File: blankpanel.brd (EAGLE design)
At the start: 140 x 183 mm, 100 parts, among them J1 S1911-46R, J3 S1911-46R, Q1 NDS8434, Q2 NDS8434, U1 ATWINC, U2 INA219, U3 ATWINC, U4 MCP7384X, U5 INA219, U6 MCP7384X

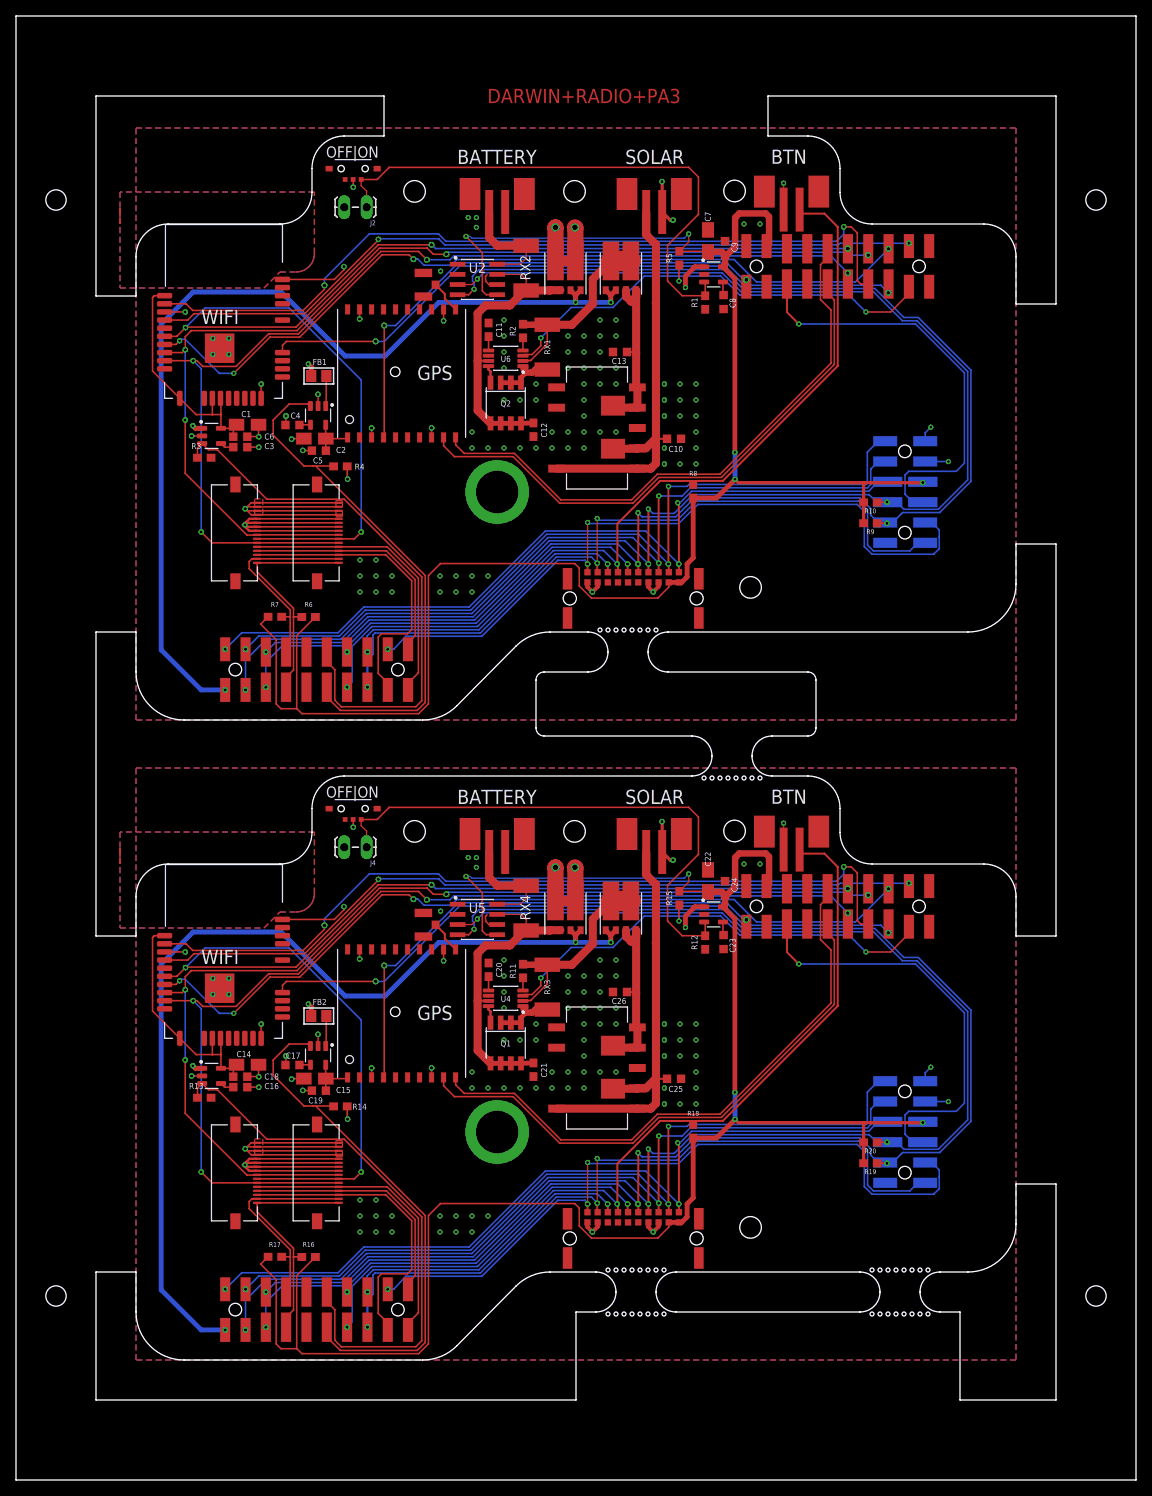
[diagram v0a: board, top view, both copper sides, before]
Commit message: Removed unwanted panel files and changed unpopulated panel template.
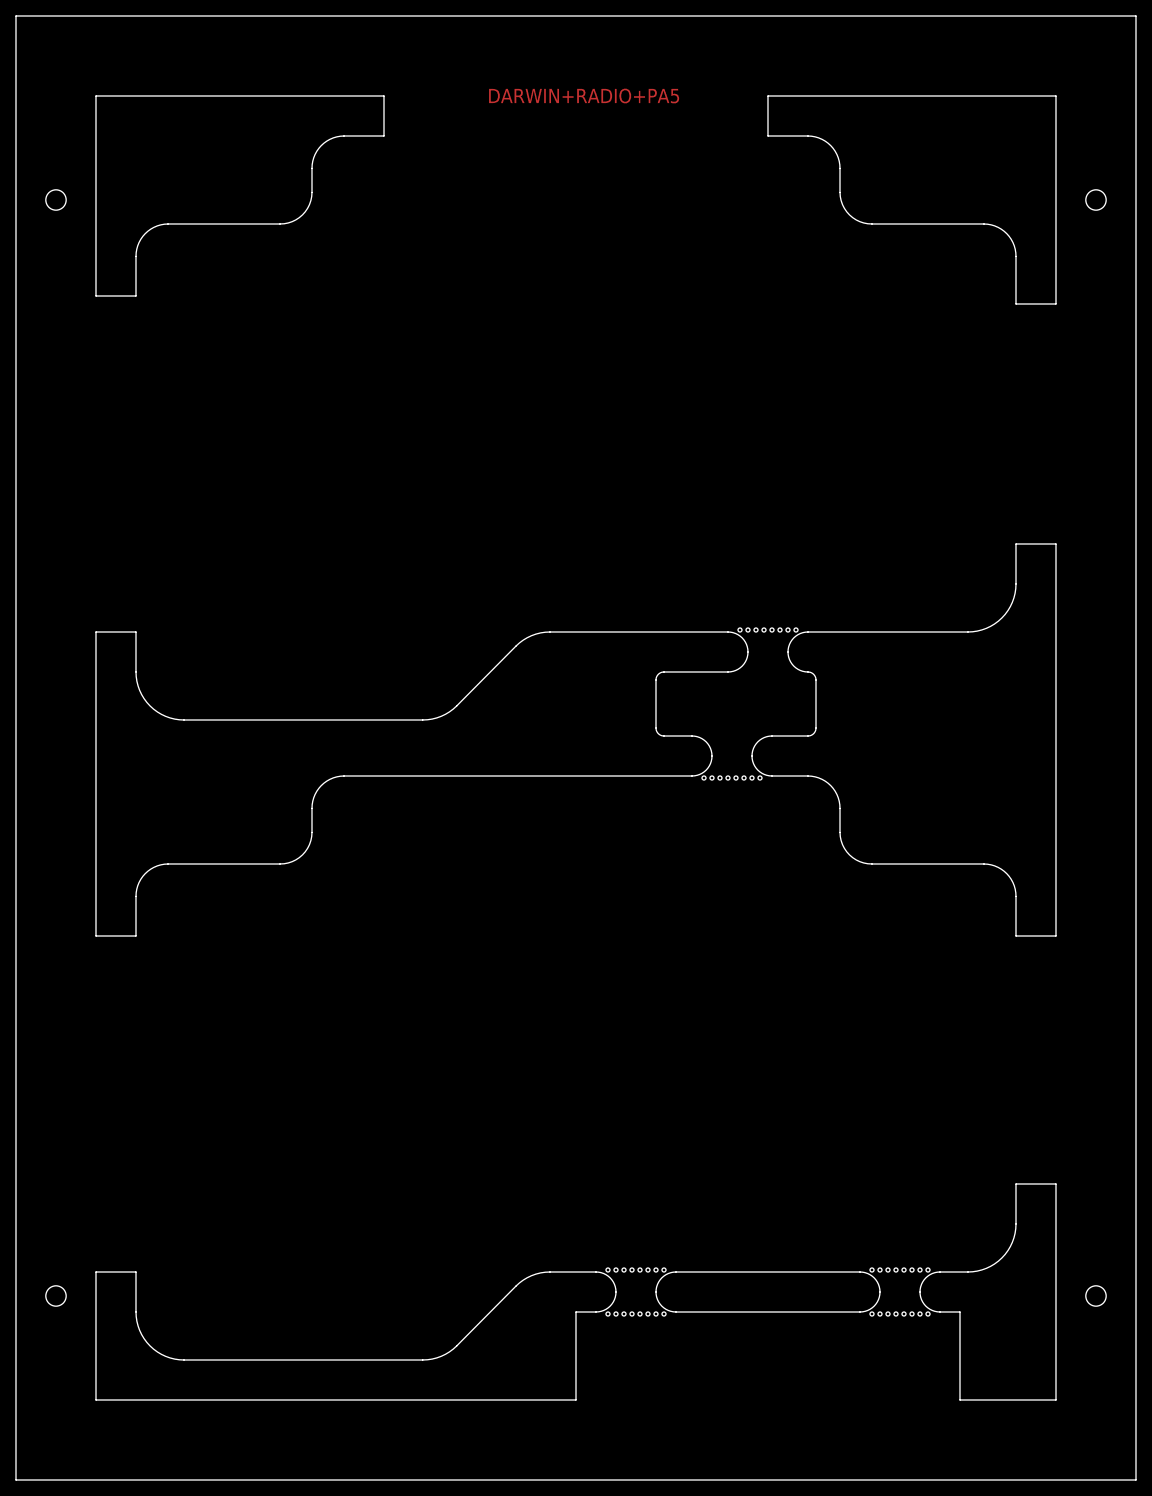
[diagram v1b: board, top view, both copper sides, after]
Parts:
- removed BACKPACK, BACKPACK1: 2X6-HEADERSDS, Conservify:12PH
- removed BACKPLANE, BACKPLANE1: M55-6102042R, Conservify:M55-6102042R
- removed BAT-JST, BAT-JST1, BTN-JST, BTN-JST1, SOLAR-JST, SOLAR-JST1: B2B-PH-SM4-TB, Conservify:B2B-PH-SM4-TB
- removed C1, C14, C15, C2, C22, C7: 6.8uf, rcl:A/3216-18R
- removed C10, C13, C25, C26: 22uf, rcl:C0603K
- removed C11, C20: 0.1uF, SparkFun-Capacitors:0603
- removed C12, C21: 10uF, SparkFun-Capacitors:0603
- removed C16, C17, C23, C3, C4, C8: 470pf, rcl:C0603K
- removed C18, C19, C24, C5, C6, C9: .1uf, rcl:C0603K
- removed D1, D2, D3, D4: V10KL45DUHM3/H, Conservify:V10KL45DUHM3/H
- removed FB1, FB2: (no value), microbuilder:0805
- removed FFC1, FFC2, FFC3, FFC4: 505110-1692, Conservify:505110-1692
- removed J1, J3: S1911-46R, Conservify:S1911-46R
- removed J2, J4: (no value), SparkFun-Connectors:1X02_LOCK_LONGPADS
- removed LOWER1, LOWER2, UPPER1, UPPER2: MOLEX-15-91-2200, Conservify:20PH
- removed Q1, Q2: NDS8434, Conservify:SO08-IRF
- removed R1, R10, R11, R12, R13, R14, R15, R16, R17, R18, R19, R2, R20, R3, R4, R5, R6, R7, R8, R9: 100k, SparkFun-Resistors:0603
- removed REG1, REG2: V78E06-1000-SMT-TR, Conservify:V78E06-1000-SMT-TR
- removed RX1, RX2, RX3, RX4: 100M, rcl:R2512
- removed U$1, U$6: FGPMMOPA6H, Conservify:GPS_MODULE
- removed U$10, U$5: SSAJ110100, Conservify:SSAJ110100
- removed U$11, U$12: 2337019-1, Conservify:2337019-1
- removed U$2, U$3, U$4, U$7, U$8, U$9: MIC5219-3.3YM5-TR, Conservify:SOT95P280X145-5
- removed U1, U3: ATWINC, Conservify:ATWINC
- removed U2, U5: INA219, Conservify:SOIC127P599X175-8N
- removed U4, U6: MCP7384X, Conservify:SOP65P490X110-8
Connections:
- removed net 3V1: BACKPACK1.3, BACKPLANE1.P11, BACKPLANE1.P12, C22.+, C24.1, R15.1, R16.2, R17.2, R18.1, R19.2, R20.2, U$9.5, U5.5, UPPER2.PIN19
- removed net 3V3: BACKPACK.3, BACKPLANE.P11, BACKPLANE.P12, C7.+, C9.1, R10.2, R5.1, R6.2, R7.2, R8.1, R9.2, U$4.5, U2.5, UPPER1.PIN19
- removed net BACKPACK_ENABLE: BACKPACK.4, UPPER1.PIN3
- removed net BACKPACK_ENABLE1: BACKPACK1.4, UPPER2.PIN3
- removed net BAT+: C12.1, D1.A1-1, D1.A1-2, Q2.5, Q2.6, Q2.7, Q2.8, RX2.1, U2.7, U6.7
- removed net BAT+1: C21.1, D2.A1-1, D2.A1-2, Q1.5, Q1.6, Q1.7, Q1.8, RX4.1, U4.7, U5.7
- removed net BAT+RAW: BAT-JST.+, RX2.2, U2.8
- removed net BAT+RAW1: BAT-JST1.+, RX4.2, U5.8
- removed net CHARGESUPPLY: D3.K1, D3.K2, R2.1, RX1.1, U6.2
- removed net CHARGESUPPLY1: D4.K1, D4.K2, R11.1, RX3.1, U4.2
- removed net CHARGING: R5.2, U6.3, UPPER1.PIN9
- removed net CHARGING1: R15.2, U4.3, UPPER2.PIN9
- removed net D+: LOWER1.PIN6
- removed net D+1: LOWER2.PIN6
- removed net D-: LOWER1.PIN15
- removed net D-1: LOWER2.PIN15
- removed net EEPROM_PROT: BACKPACK.5, BACKPLANE.P1, LOWER1.PIN2
- removed net EEPROM_PROT1: BACKPACK1.5, BACKPLANE1.P1, LOWER2.PIN2
- removed net GND: BACKPACK.2, BACKPLANE.P19, BACKPLANE.P20, BAT-JST.-, BTN-JST.+, C1.-, C10.2, C11.2, C12.2, C13.2, C2.-, C3.2, C4.2, C5.2, C6.2, C7.-, C8.2, C9.2, FFC1.1, FFC1.2, FFC1.3, FFC1.4, FFC2.1, FFC2.2, FFC2.3, FFC2.4, R1.1, R3.1, R4.1, REG1.P$3, REG1.P$7, SOLAR-JST.-, U$1.P$12, U$1.P$19, U$1.P$3, U$1.P$8, U$11.GND, U$11.GND2, U$2.2, U$3.2, U$4.2, U1.12, U1.28, U1.9, U1.PAD, U2.1, U2.2, U2.6, U6.6, UPPER1.PIN20
- removed net GND2: BACKPACK1.2, BACKPLANE1.P19, BACKPLANE1.P20, BAT-JST1.-, BTN-JST1.+, C14.-, C15.-, C16.2, C17.2, C18.2, C19.2, C20.2, C21.2, C22.-, C23.2, C24.2, C25.2, C26.2, FFC3.1, FFC3.2, FFC3.3, FFC3.4, FFC4.1, FFC4.2, FFC4.3, FFC4.4, R12.1, R13.1, R14.1, REG2.P$3, REG2.P$7, SOLAR-JST1.-, U$12.GND, U$12.GND2, U$6.P$12, U$6.P$19, U$6.P$3, U$6.P$8, U$7.2, U$8.2, U$9.2, U3.12, U3.28, U3.9, U3.PAD, U4.6, U5.1, U5.2, U5.6, UPPER2.PIN20
- removed net GPS_ENABLE: LOWER1.PIN16, R4.2, U$2.3
- removed net GPS_ENABLE1: LOWER2.PIN16, R14.2, U$7.3
- removed net GPS_RX: U$1.P$9, UPPER1.PIN5
- removed net GPS_RX1: U$6.P$9, UPPER2.PIN5
- removed net GPS_TX: U$1.P$10, UPPER1.PIN16
- removed net GPS_TX1: U$6.P$10, UPPER2.PIN16
- removed net HOTSWAP_INT: BACKPLANE.P3, LOWER1.PIN3
- removed net HOTSWAP_INT1: BACKPLANE1.P3, LOWER2.PIN3
- removed net MOD_G0: FFC1.13, FFC2.13, LOWER1.PIN1
- removed net MOD_G1: FFC3.13, FFC4.13, LOWER2.PIN1
- removed net MOD_G13: FFC1.14, FFC2.14, LOWER1.PIN19
- removed net MOD_G14: FFC1.12, FFC2.12, LOWER1.PIN20
- removed net MOD_G2: BACKPACK.6, BACKPLANE.P2, LOWER1.PIN18
- removed net MOD_G3: BACKPACK1.6, BACKPLANE1.P2, LOWER2.PIN18
- removed net MOD_G4: BACKPLANE1.P5, LOWER2.PIN4
- removed net MOD_G5: BACKPLANE.P5, LOWER1.PIN4
- removed net MOD_G6: FFC3.14, FFC4.14, LOWER2.PIN19
- removed net MOD_G7: FFC3.12, FFC4.12, LOWER2.PIN20
- removed net MOD_MISO: BACKPACK.10, BACKPLANE.P10, LOWER1.PIN10
- removed net MOD_MISO1: BACKPACK1.10, BACKPLANE1.P10, LOWER2.PIN10
- removed net MOD_MOSI: BACKPACK.11, BACKPLANE.P8, LOWER1.PIN12
- removed net MOD_MOSI1: BACKPACK1.11, BACKPLANE1.P8, LOWER2.PIN12
- removed net MOD_SCK: BACKPACK.12, BACKPLANE.P9, LOWER1.PIN9
- removed net MOD_SCK1: BACKPACK1.12, BACKPLANE1.P9, LOWER2.PIN9
- removed net MOD_SCL: BACKPACK.8, BACKPLANE.P6, LOWER1.PIN13, R9.1, U2.4
- removed net MOD_SCL1: BACKPACK1.8, BACKPLANE1.P6, LOWER2.PIN13, R19.1, U5.4
- removed net MOD_SDA: BACKPACK.9, BACKPLANE.P7, LOWER1.PIN8, R10.1, U2.3
- removed net MOD_SDA1: BACKPACK1.9, BACKPLANE1.P7, LOWER2.PIN8, R20.1, U5.3
- removed net N$1: C3.1, U$3.4
- removed net N$11: C17.1, U$7.4
- removed net N$12: C15.+, C19.1, U$6.P$1, U$7.5
- removed net N$13: Q1.1, Q1.2, Q1.3, RX3.2, U4.1
- removed net N$14: Q2.1, Q2.2, Q2.3, RX1.2, U6.1
- removed net N$16: Q1.4, U4.8
- removed net N$17: Q2.4, U6.8
- removed net N$18: C11.1, U6.5
- removed net N$19: C20.1, U4.5
- removed net N$2: C4.1, U$2.4
- removed net N$20: R11.2, U4.4
- removed net N$21: C23.1, U$9.4
- removed net N$22: U$12.ANT, U$6.P$11
- removed net N$23: FB2.2, U$7.1
- removed net N$3: C2.+, C5.1, U$1.P$1, U$2.5
- removed net N$4: U$1.P$11, U$11.ANT
- removed net N$5: R2.2, U6.4
- removed net N$6: C8.1, U$4.4
- removed net N$7: FB1.2, U$2.1
- removed net N$8: C16.1, U$8.4
- removed net PIN1: BACKPACK1.7
- removed net PIN7: BACKPACK.7
- removed net PSWITCH: J2.1, R1.2, U$4.3, U$5.2
- removed net PSWITCH1: J4.1, R12.2, U$10.2, U$9.3
- removed net RADIO_MISO: FFC1.9, FFC2.9, U1.17, UPPER1.PIN14
- removed net RADIO_MISO1: FFC3.9, FFC4.9, U3.17, UPPER2.PIN14
- removed net RADIO_MOSI: FFC1.10, FFC2.10, U1.15, UPPER1.PIN15
- removed net RADIO_MOSI1: FFC3.10, FFC4.10, U3.15, UPPER2.PIN15
- removed net RADIO_SCK: FFC1.11, FFC2.11, U1.18, UPPER1.PIN6
- removed net RADIO_SCK1: FFC3.11, FFC4.11, U3.18, UPPER2.PIN6
- removed net RAD_SCL: FFC1.16, FFC2.16, LOWER1.PIN14, R6.1
- removed net RAD_SCL1: FFC3.16, FFC4.16, LOWER2.PIN14, R16.1
- removed net RAD_SDA: FFC1.15, FFC2.15, LOWER1.PIN7, R7.1
- removed net RAD_SDA1: FFC3.15, FFC4.15, LOWER2.PIN7, R17.1
- removed net RESET: UPPER1.PIN4
- removed net RESET1: UPPER2.PIN4
- removed net SOL+: C10.1, J1.P$2, REG1.P$1, REG1.P$10, REG1.P$2, SOLAR-JST.+
- removed net SOL+1: C25.1, J3.P$2, REG2.P$1, REG2.P$10, REG2.P$2, SOLAR-JST1.+
- removed net SOLREG: C13.1, D3.A2-1, D3.A2-2, J1.P$1, REG1.P$4, REG1.P$5
- removed net SOLREG1: C26.1, D4.A2-1, D4.A2-2, J3.P$1, REG2.P$4, REG2.P$5
- removed net SWCLK: UPPER1.PIN10
- removed net SWCLK1: UPPER2.PIN10
- removed net SWDIO: UPPER1.PIN11
- removed net SWDIO1: UPPER2.PIN11
- removed net UNREG: BACKPACK.1, BACKPLANE.P13, BACKPLANE.P14, D1.K1, D1.K2, FB1.1, FFC1.5, FFC1.6, FFC1.7, FFC1.8, FFC2.5, FFC2.6, FFC2.7, FFC2.8, J2.2, U$3.1, U$4.1, U$5.C
- removed net UNREG1: BACKPACK1.1, BACKPLANE1.P13, BACKPLANE1.P14, D2.K1, D2.K2, FB2.1, FFC3.5, FFC3.6, FFC3.7, FFC3.8, FFC4.5, FFC4.6, FFC4.7, FFC4.8, J4.2, U$10.C, U$8.1, U$9.1
- removed net V1: D2.A2-1, D2.A2-2, D4.A1-1, D4.A1-2, LOWER2.PIN11
- removed net V5: D1.A2-1, D1.A2-2, D3.A1-1, D3.A1-2, LOWER1.PIN11
- removed net VBACKUP: U$1.P$4, UPPER1.PIN1
- removed net VBACKUP1: U$6.P$4, UPPER2.PIN1
- removed net WIFI_3V1: C14.+, C18.1, U$8.5, U3.10, U3.20, U3.22, U3.23
- removed net WIFI_3V3: C1.+, C6.1, U$3.5, U1.10, U1.20, U1.22, U1.23
- removed net WIFI_CS: U1.16, UPPER1.PIN13
- removed net WIFI_CS1: U3.16, UPPER2.PIN13
- removed net WIFI_ENABLE: LOWER1.PIN5, R3.2, U$3.3
- removed net WIFI_ENABLE1: LOWER2.PIN5, R13.2, U$8.3
- removed net WIFI_IRQ: U1.13, UPPER1.PIN12
- removed net WIFI_IRQ1: U3.13, UPPER2.PIN12
- removed net WIFI_RST: U1.4, UPPER1.PIN8
- removed net WIFI_RST1: U3.4, UPPER2.PIN8
- removed net WIFI_WAKE: U1.11, UPPER1.PIN7
- removed net WIFI_WAKE1: U3.11, UPPER2.PIN7
- removed net X1: UPPER2.PIN2
- removed net X2: UPPER1.PIN2
- removed net X3: UPPER2.PIN17
- removed net X4: UPPER1.PIN17
- removed net X5: UPPER1.PIN18
- removed net X6: UPPER2.PIN18
- removed net XBTN: BACKPLANE.P4, BTN-JST.-, LOWER1.PIN17, R8.2
- removed net XBTN1: BACKPLANE1.P4, BTN-JST1.-, LOWER2.PIN17, R18.2
- removed net XX1: BACKPLANE.P18
- removed net XX2: BACKPLANE.P17
- removed net XX3: BACKPLANE.P16
- removed net XX4: BACKPLANE.P15
- removed net XX5: BACKPLANE1.P16
- removed net XX6: BACKPLANE1.P18
- removed net XX7: BACKPLANE1.P17
- removed net XX8: BACKPLANE1.P15
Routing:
- net 3V3: track 232.1 -> 0.00 mm, vias 5 -> 0
- net 3V1: track 232.1 -> 0.00 mm, vias 5 -> 0
- net MOD_SCL1: track 198.1 -> 0.00 mm, vias 5 -> 0
- net MOD_SCL: track 198.1 -> 0.00 mm, vias 5 -> 0
- net MOD_SDA: track 190.3 -> 0.00 mm, vias 5 -> 0
- net MOD_SDA1: track 190.3 -> 0.00 mm, vias 5 -> 0
- net RADIO_MOSI1: track 149.4 -> 0.00 mm, vias 5 -> 0
- net RADIO_MOSI: track 149.4 -> 0.00 mm, vias 5 -> 0
- net RADIO_SCK1: track 132.7 -> 0.00 mm, vias 4 -> 0
- net RADIO_SCK: track 132.7 -> 0.00 mm, vias 4 -> 0
- net RADIO_MISO1: track 132.7 -> 0.00 mm, vias 4 -> 0
- net RADIO_MISO: track 132.7 -> 0.00 mm, vias 4 -> 0
- net V1: track 120.9 -> 0.00 mm, vias 3 -> 0
- net V5: track 120.9 -> 0.00 mm, vias 3 -> 0
- net XBTN: track 109.4 -> 0.00 mm, vias 2 -> 0
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- removed copper zone on layer 1, net GND
- removed copper zone on layer 16, net GND
- removed copper zone on layer 1, net GND1
- removed copper zone on layer 1, net GND2
- removed copper zone on layer 16, net GND2
- removed copper zone on layer 1, net GND3
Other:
- outline, holes or cut-outs redrawn
- board text added: "DARWIN+RADIO+PA5"
- board text removed: "BATTERY"
- board text removed: "BTN"
- board text removed: "C1"
- board text removed: "C10"
- board text removed: "C11"
- board text removed: "C12"
- board text removed: "C13"
- board text removed: "C2"
- board text removed: "C3"
- board text removed: "C4"
- board text removed: "C5"
- board text removed: "C6"
- board text removed: "C7"
- board text removed: "C8"
- board text removed: "C9"
- board text removed: "DARWIN+RADIO+PA3"
- board text removed: "FB1"
- board text removed: "GPS"
- board text removed: "J2"
- board text removed: "OFF|ON"
- board text removed: "Q2"
- board text removed: "R1"
- board text removed: "R10"
- board text removed: "R2"
- board text removed: "R3"
- board text removed: "R4"
- board text removed: "R5"
- board text removed: "R6"
- board text removed: "R7"
- board text removed: "R8"
- board text removed: "R9"
- board text removed: "RX1"
- board text removed: "RX2"
- board text removed: "SOLAR"
- board text removed: "U2"
- board text removed: "U6"
- board text removed: "WIFI"
